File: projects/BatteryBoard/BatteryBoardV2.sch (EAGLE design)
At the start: 210 parts, among them M1 BSO201SP, SW1 BTS50015-1TAD, SW2 BTS50015-1TAD, T1 AD590FLATPACK, T2 AD590FLATPACK, T3 AD590FLATPACK, T4 AD590FLATPACK, U1 TCA9535PWR, U10 LT1962-3, U11 LT1962-3, U12 LTC4411, U13 LTC4411, U14 LTC4121, U15 VNS3NV04DP-E, U16 LTC4121, U17 VNS3NV04DP-E, U2 AD7991-0, U3 LTC4412MPS6, U4 LTC4121-4.2, U5 LTC4121-4.2, U6 LC05111C13MTTTG, U7 LC05111C13MTTTG, U8 AD8418, U9 AD8418

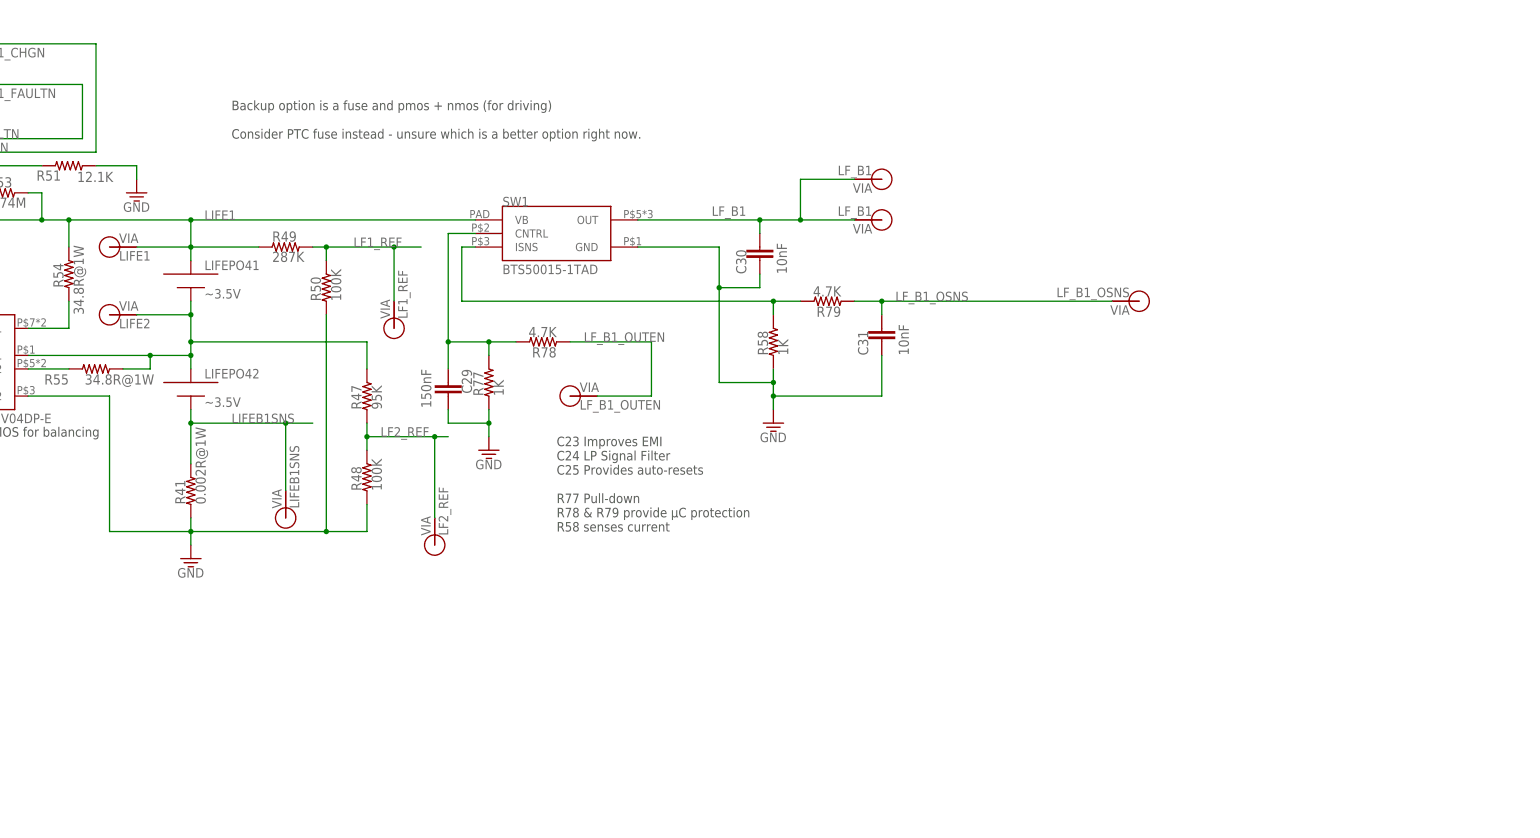
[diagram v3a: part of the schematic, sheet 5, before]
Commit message: Added #2 MTG part to BSE libary. Added 2016L PTC fuse part to BSE library. Adjusted BSE libary part descriptions. Added net classes, lifepo current sense and fusing, schematic clean up, mounting parts, and initial board layout for large components to Battery Board V2.
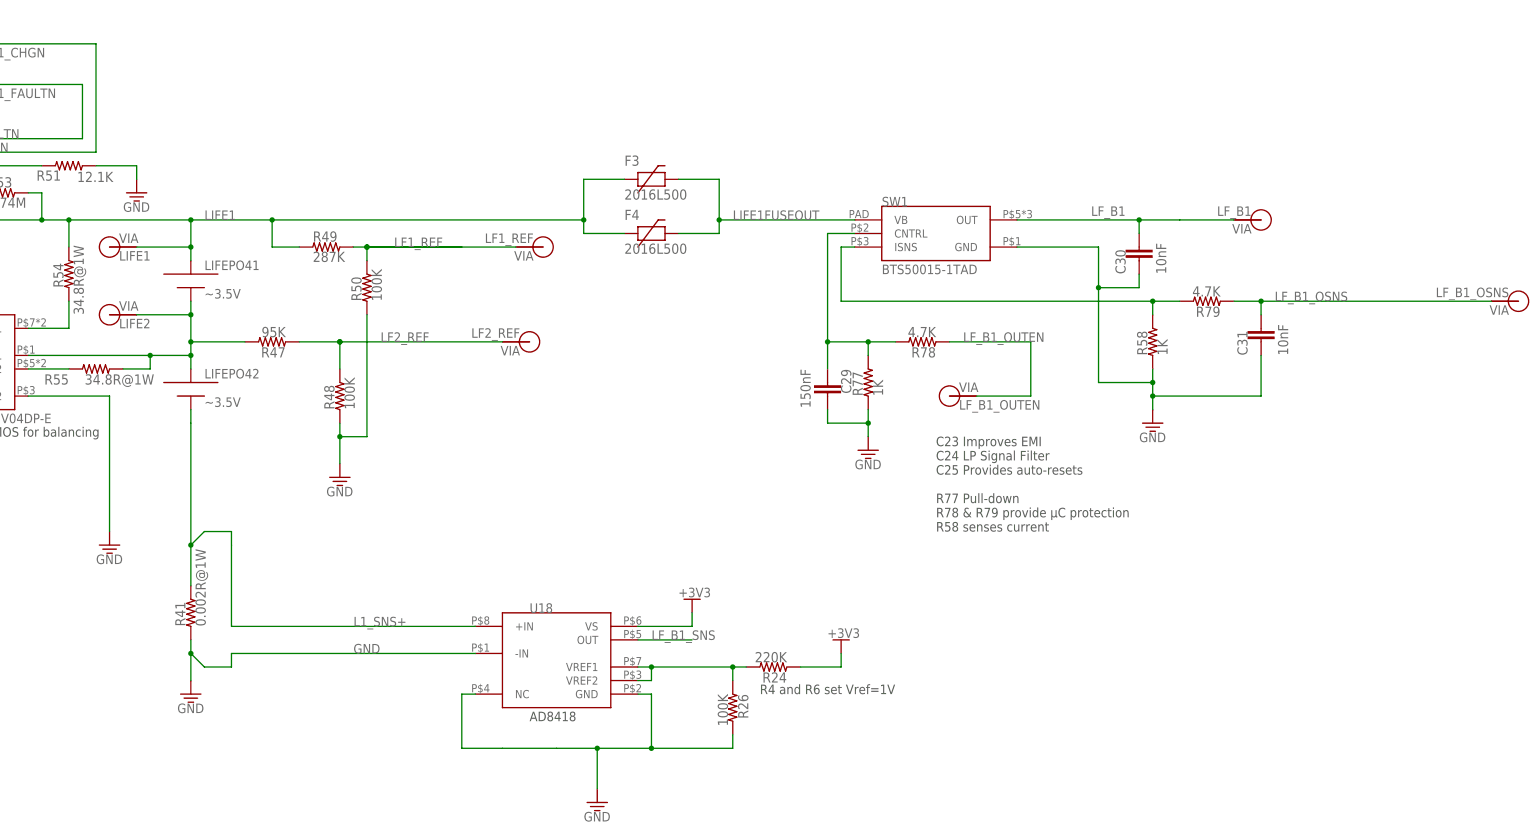
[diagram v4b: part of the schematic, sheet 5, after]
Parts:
- removed V40: LIFEB1SNS, BrownSpaceEngineering:VIA-60MIL
- removed V44: LF_B1, BrownSpaceEngineering:VIA-120MIL
- removed V48: LF_B2_SNS, BrownSpaceEngineering:VIA-60MIL
- removed V52: LIFE_B2, BrownSpaceEngineering:VIA-120MIL
- added F3, F4, F5, F6: 2016L500, BrownSpaceEngineering:2016L500
- added MTG1, MTG2, MTG3, MTG4: (no value), BrownSpaceEngineering:MTG-NPTH-#2-CLOSE
- added R24, R29: 220K, BrownSpaceEngineering:RES0805
- added R26, R30: 100K, BrownSpaceEngineering:RES0805
- added U18, U19: AD8418, BrownSpaceEngineering:AD8418
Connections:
- removed net LIFEB1SNS: LIFEPO42.MINUS, R41.2, V40.P$1
- new net LF_B1_SNS: U18.OUT
- new net LIFE1FUSEOUT: F3.P$2, F4.P$2, SW1.VB
- new net LIFE3FUSEOUT: F5.P$2, F6.P$2, SW2.VB
- new net N$10: R29.2, R30.1, U19.VREF1, U19.VREF2
- new net N$11: R24.2, R26.1, U18.VREF1, U18.VREF2
- net +3V3: now also R24.1, R29.1, U18.VS, U19.VS
- net GND: now also R26.2, R30.2, U18.-IN, U18.GND, U18.NC, U19.-IN, U19.GND, U19.NC
- net L1_SNS+: now also LIFEPO42.MINUS, LIFEPO44.MINUS, R41.2, R59.2, U18.+IN, U19.+IN
- net LF_B1: no longer V44.P$1
- net LF_B2_SNS: now also U19.OUT; no longer LIFEPO44.MINUS, R59.2, V48.P$1
- net LIFE1: now also F3.P$1, F4.P$1; no longer SW1.VB
- net LIFE3: now also F5.P$1, F6.P$1; no longer SW2.VB
- net LIFE_B2: no longer V52.P$1
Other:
- note removed: "Backup option is a fuse and pmos + nmos (for driving) Consider PTC fuse instead - unsure which is a better option right now."
- moved on the sheet: C29, C30, C31, C36, C37, C38, R33, R34, R41, R47, R48, R49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

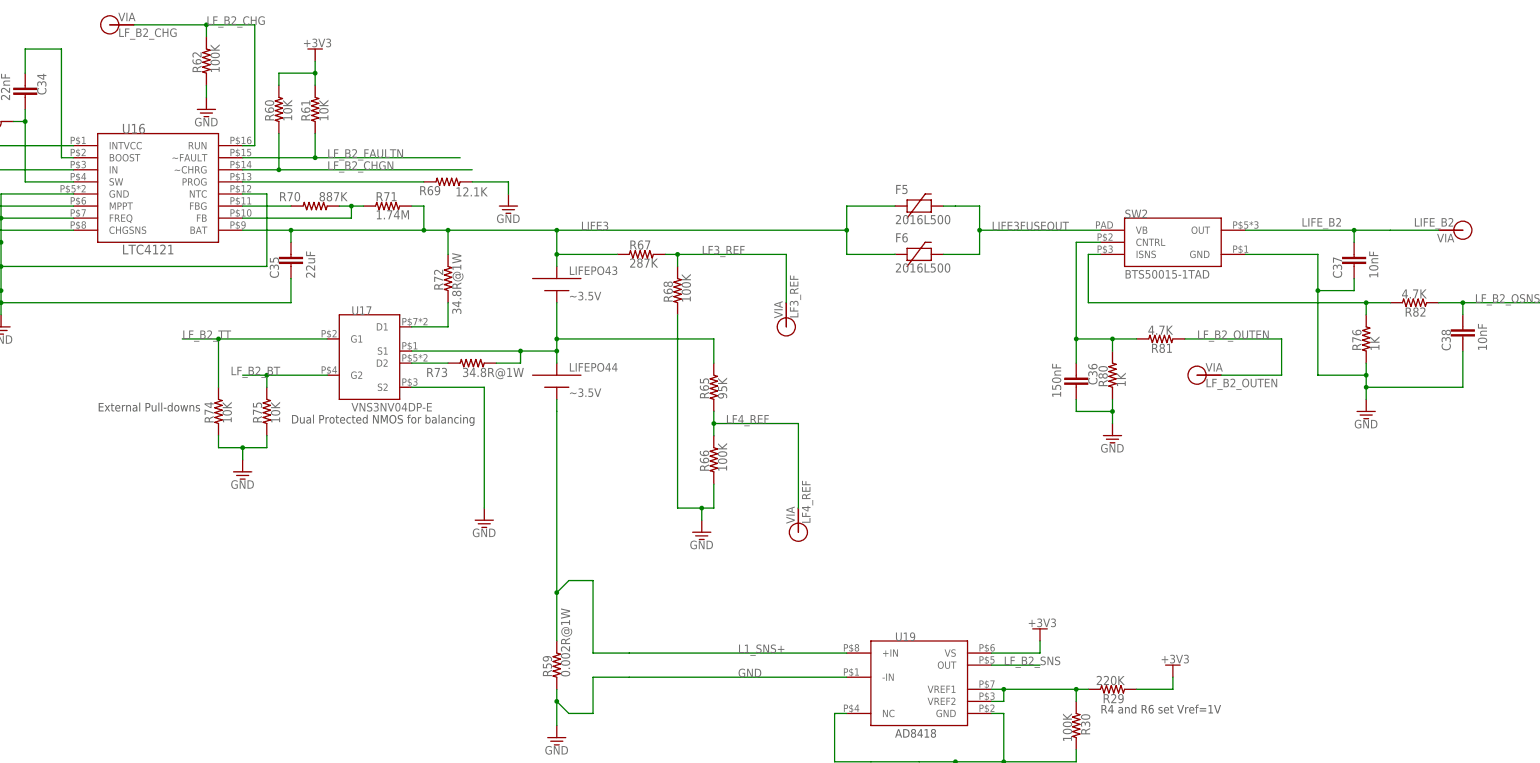
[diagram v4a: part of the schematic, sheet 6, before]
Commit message: Addition of zener diodes. Updates to some resistor values. Inital layout of all Li-ion circuitry.
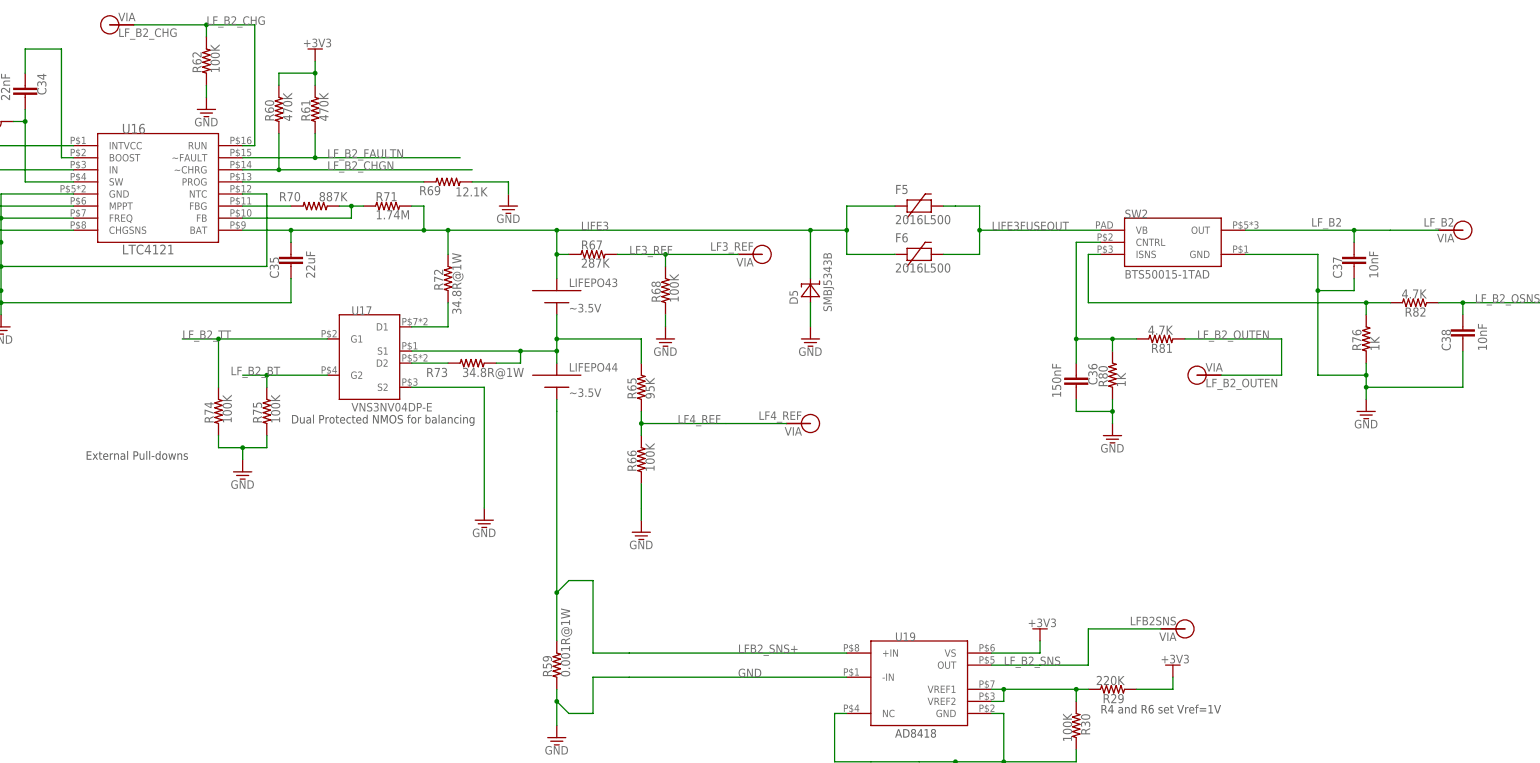
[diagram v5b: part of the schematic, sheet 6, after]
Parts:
- removed V32: L2_ST, BrownSpaceEngineering:VIA-60MIL
- added D4, D5: SMBJ5343B, BattBoard:SMBJ5343B
- added V40: LFB1SNS, BrownSpaceEngineering:VIA-60MIL
- added V44: LFB2SNS, BrownSpaceEngineering:VIA-60MIL
- R39: value 150K -> 15K
- R40: value 100K -> 10K
- R41, R59: value 0.002R@1W -> 0.001R@1W
- R42, R43, R60, R61: value 10K -> 470K
- R56, R57, R74, R75: value 10K -> 100K
- V31: value L1_ST -> L2_REF
- V33: value L_OUT -> L2_CHG; device BrownSpaceEngineering:VIA-120MIL -> BrownSpaceEngineering:VIA-60MIL
- V53: value LIFE_B2 -> LF_B2
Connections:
- net LIFE_B2 renamed LF_B2
- new net LFB1_SNS+: LIFEPO42.MINUS, R41.2, U18.+IN
- new net LFB2_SNS+: LIFEPO44.MINUS, R59.2, U19.+IN
- net GND: now also D4.A, D5.A
- net L1_SNS+: no longer LIFEPO42.MINUS, LIFEPO44.MINUS, R41.2, R59.2, U18.+IN, U19.+IN
- net L1_ST: no longer V31.P$1
- net L2_CHG: now also V33.P$1
- net L2_REF: now also V31.P$1
- net L2_ST: no longer V32.P$1
- net LF_B1_SNS: now also V40.P$1
- net LF_B2_SNS: now also V44.P$1
- net LIFE1: now also D4.C
- net LIFE3: now also D5.C
- net L_OUT: no longer V33.P$1
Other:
- note added: "AD8418 has 20V/V gain"
- note added: "Input impedance of ADC = 69K R14//Input = 8.734K Voltage divider ratio: 0.1792V(in)/V(actual)"
- note added: "Input impedance of ADC = 69K R14//Input = 8.734K Voltage divider ratio: 0.368V(in)/V(actual)"
- note added: "PMR25HZPFV1L00"
- note added: "Sense Resistor has 2.5x power rating <2s"
- moved on the sheet: LIFEPO43, R25, R49, R65, R66, R67, R68

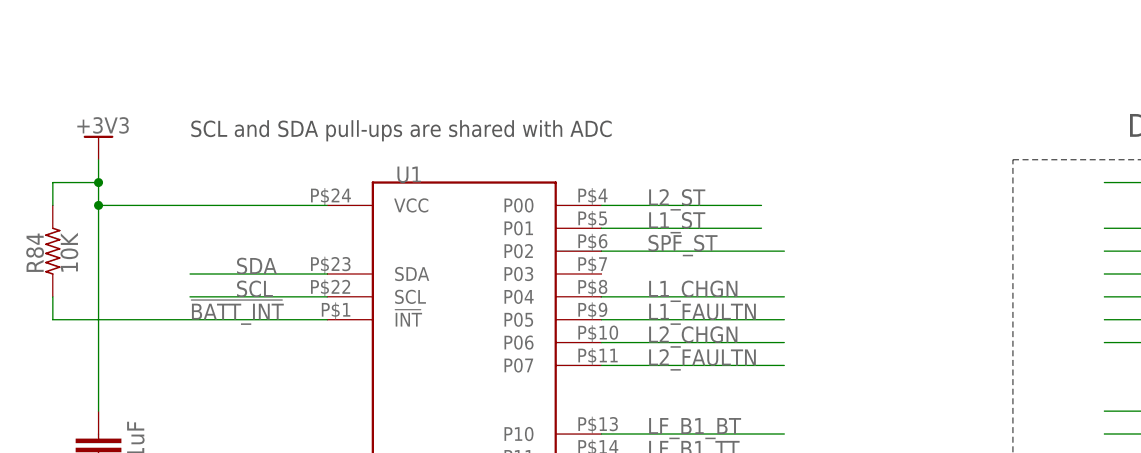
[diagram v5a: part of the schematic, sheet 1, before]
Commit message: Finished inital placement of all components on the battery board. Updated pull-down values for high-side switch input resistor.
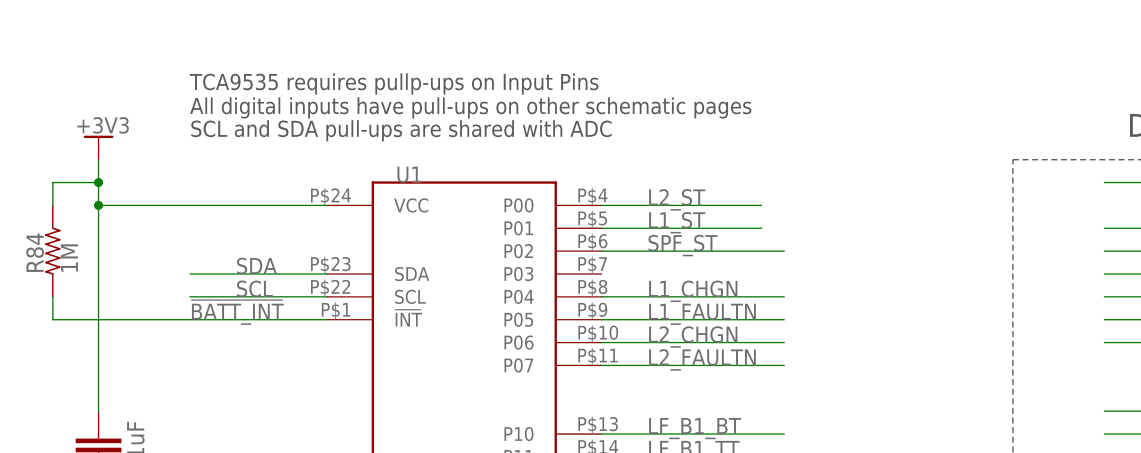
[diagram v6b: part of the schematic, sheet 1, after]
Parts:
- R77, R80: value 1K -> 100K
- R84: value 10K -> 1M
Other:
- note added: "TCA9535 requires pullp-ups on Input Pins All digital inputs have pull-ups on other schematic pages"
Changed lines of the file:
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@@
 <part name="GND2" library="supply1" deviceset="GND" device=""/>
 <part name="SW1" library="BrownSpaceEngineering" deviceset="BTS50015-1TAD" device=""/>
-<part name="R77" library="BrownSpaceEngineering" deviceset="RES" device="0805" value="1K"/>
+<part name="R77" library="BrownSpaceEngineering" deviceset="RES" device="0805" value="100K"/>
 <part name="R78" library="BrownSpaceEngineering" deviceset="RES" device="0805" value="4.7K"/>
 <part name="R79" library="BrownSpaceEngineering" deviceset="RES" device="0805" value="4.7K"/>
@@
 <part name="GND45" library="supply1" deviceset="GND" device=""/>
 <part name="SW2" library="BrownSpaceEngineering" deviceset="BTS50015-1TAD" device=""/>
-<part name="R80" library="BrownSpaceEngineering" deviceset="RES" device="0805" value="1K"/>
+<part name="R80" library="BrownSpaceEngineering" deviceset="RES" device="0805" value="100K"/>
 <part name="R81" library="BrownSpaceEngineering" deviceset="RES" device="0805" value="4.7K"/>
 <part name="R82" library="BrownSpaceEngineering" deviceset="RES" device="0805" value="4.7K"/>
@@
 <part name="C1" library="BrownSpaceEngineering" deviceset="CAP" device="0805" value="0.1uF"/>
 <part name="C2" library="BrownSpaceEngineering" deviceset="CAP" device="0805" value="0.1uF"/>
-<part name="R84" library="BrownSpaceEngineering" deviceset="RES" device="0805" value="10K"/>
+<part name="R84" library="BrownSpaceEngineering" deviceset="RES" device="0805" value="1M"/>
 <part name="V3" library="BrownSpaceEngineering" deviceset="VIA" device="60MIL-SQ" value="GND"/>
 <part name="V4" library="BrownSpaceEngineering" deviceset="VIA" device="-120MIL" value="GND"/>
@@
 <wire x1="119.38" y1="35.56" x2="142.24" y2="35.56" width="0.1524" layer="97" style="dashdot"/>
 <text x="-93.98" y="83.82" size="1.778" layer="97">SCL and SDA pull-ups are shared with ADC</text>
+<text x="-93.98" y="86.36" size="1.778" layer="97">TCA9535 requires pullp-ups on Input Pins
+All digital inputs have pull-ups on other schematic pages</text>
 </plain>
 <instances>
